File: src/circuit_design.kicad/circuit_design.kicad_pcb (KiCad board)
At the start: 2 copper layers, 205.7 x 170.8 mm, 183 parts, among them J1 CONN_BAT, Q1 BT134-600E, Q2 BT134-600E, Q3 BT134-600E, Q4 BT134-600E, U1 К176ИЕ12, U10 К155ЛА4, U11 К155ЛИ1, U12 К155ЛА1, U13 К155ИЕ5, U14 К155ЛЛ1, U15 К155ЛН1, U16 К155ЛИ1, U17 К155ТВ15, U18 К155ИЕ5, U19 К155ЛП5, U2 К155ЛП10, U20 К155ИВ1, U21 К155ИД7, U22 К155ИД4, U23 К155ЛН1, U24 К155ЛП10, U25 MOC3062M, U26 MOC3062M, U27 MOC3062M, U28 MOC3062M, U29 LM7806_TO220, U3 К155ЛЕ3, U30 SC6038, U31 К155ЛЕ1, U32 К155ЛН1, U33 К155ЛИ1, U34 К155ЛА4, U35 К155ТВ15, U36 К155ТЛ2, U37 4020, U38 LM7806_TO220, U39 К155ЛН1, U4 К155ЛН1, U5 К155ЛИ1, U6 К155ЛЛ1, U7 4020, U8 ICL7660, U9 К155ИЕ5, Y1 32768

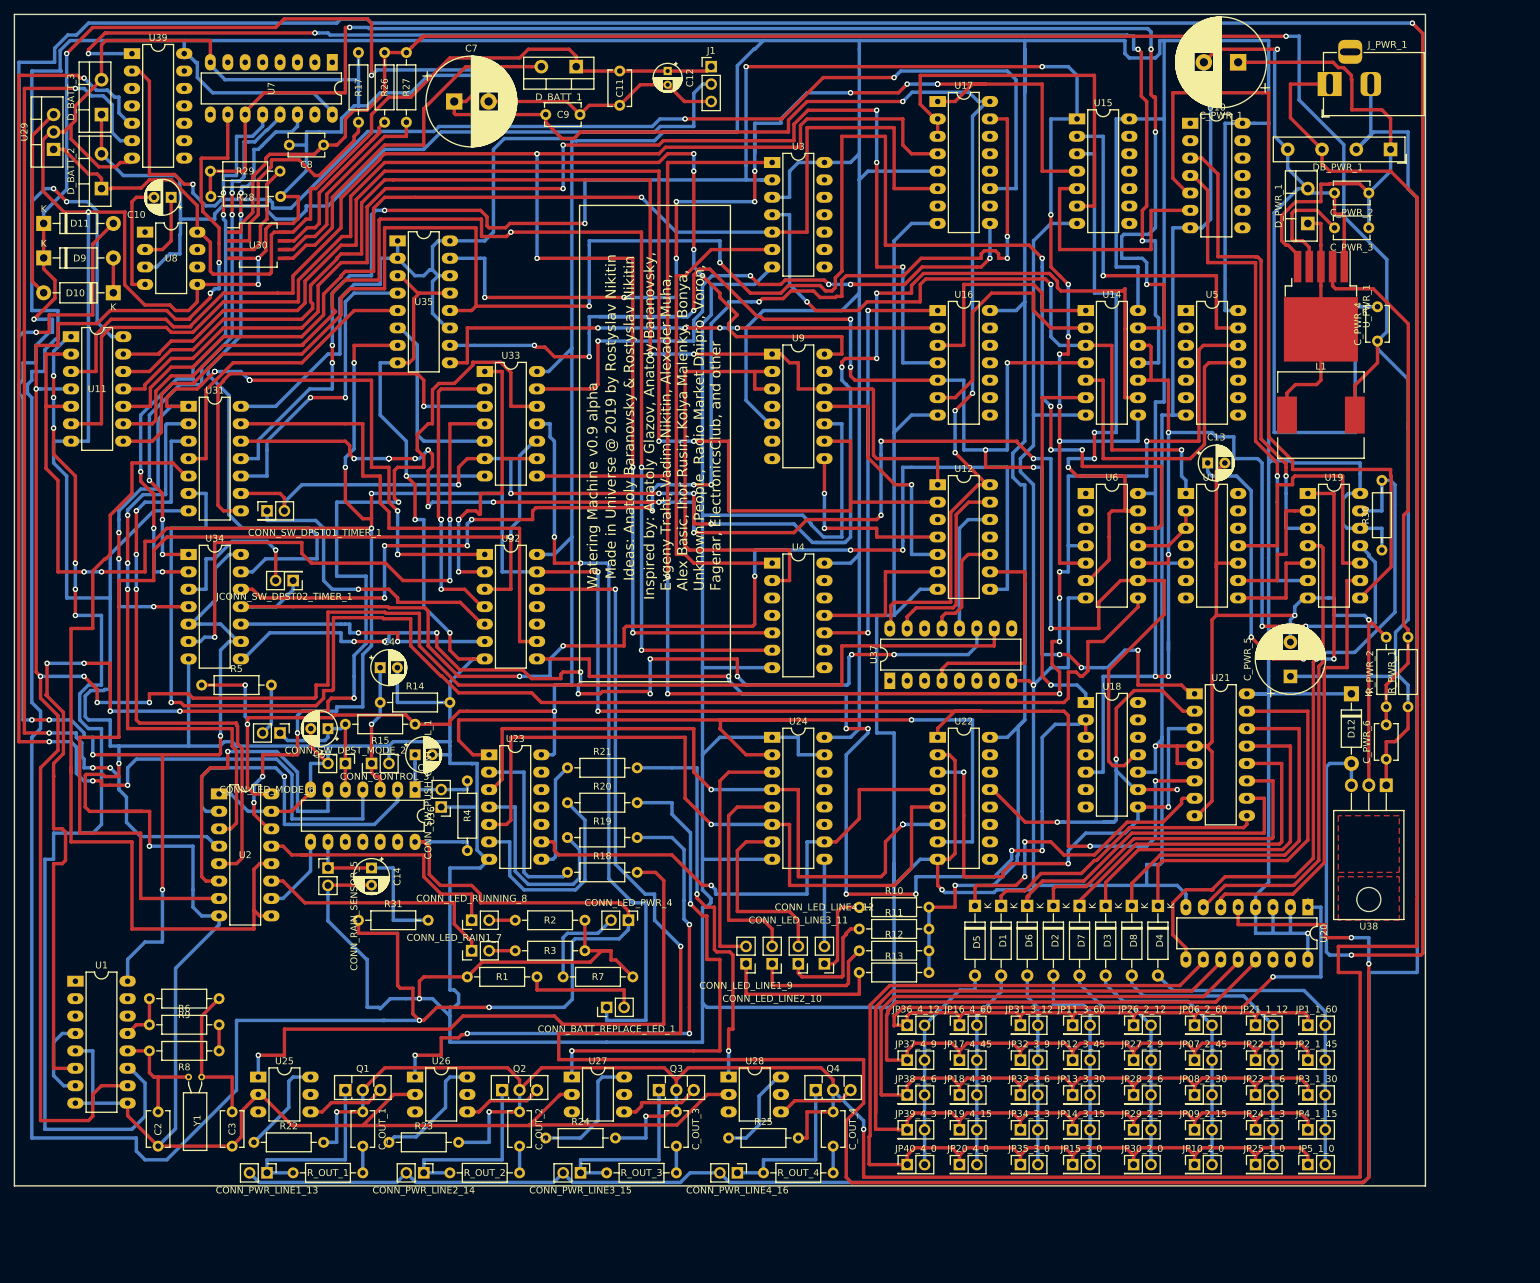
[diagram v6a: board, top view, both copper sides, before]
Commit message: The labels was updated:   - Was placed outside of the parts   - Was situated to be more readable
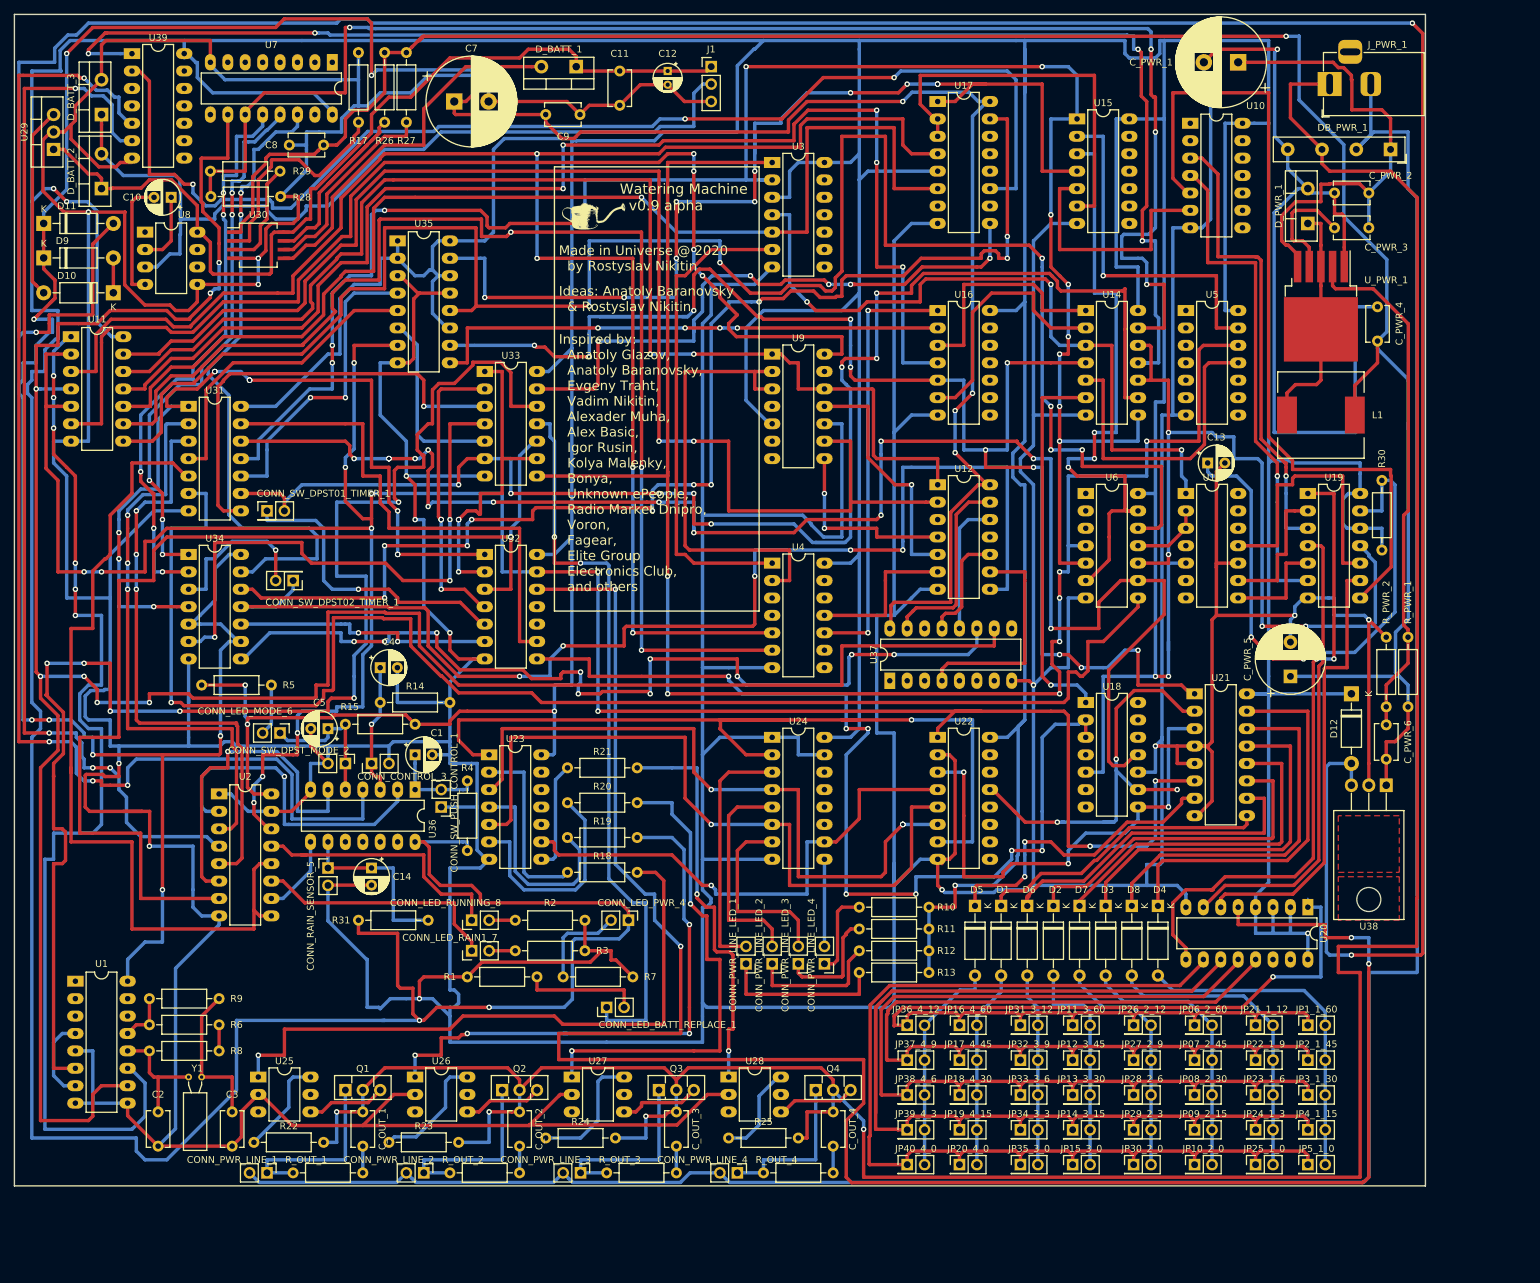
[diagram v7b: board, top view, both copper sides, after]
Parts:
- added G***: LOGO, circuit_design:logo, F.Cu at (127.6, 38.1)
- renumbered CONN_BATT_REPLACE_LED_1 to CONN_LED_BATT_REPLACE_1, CONN_PWR_LINE1_13 to CONN_PWR_LINE_1, CONN_PWR_LINE2_14 to CONN_PWR_LINE_2, CONN_PWR_LINE3_15 to CONN_PWR_LINE_3, CONN_PWR_LINE4_16 to CONN_PWR_LINE_4, CONN_LED_LINE1_9 to CONN_PWR_LINE_LED_1, CONN_LED_LINE2_10 to CONN_PWR_LINE_LED_2, CONN_LED_LINE3_11 to CONN_PWR_LINE_LED_3, CONN_LED_LINE4_12 to CONN_PWR_LINE_LED_4, JCONN_SW_DPST02_TIMER_1 to CONN_SW_DPST02_TIMER_1
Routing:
- net /D2: track 147.2 -> 144.4 mm
- net /D0: track 156.1 -> 153.3 mm
- net /D1: track 168.5 -> 165.7 mm
- net /D3: track 142.8 -> 140.1 mm
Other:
- board text added: "Inspired by: Anatoly Glazov, Anatoly Baranovsky, Evgeny Traht, Vadim Nikitin, Alexader Muha, Alex Basic, Igor Rusin, Kolya Malenky, Bonya, Unknown ePeople, Radio Market Dnipro, Voron, Fagear, Elite Group Electronics Club, and others"
- board text added: "Made in Universe @ 2020 by Rostyslav Nikitin"
- board text removed: "Inspired by: Anatoly Glazov, Anatoly Baranovsky, Evgeny Traht, Vadim Nikitin, Alexader Muha, Alex Basic, Ihor Rusin, Kolya Malenky, Bonya, Unknown People, Radio Market Dnipro, Voron, Fagerar, ElectronicsClub, and other"
- board text removed: "Made in Universe @ 2019 by Rostyslav Nikitin"

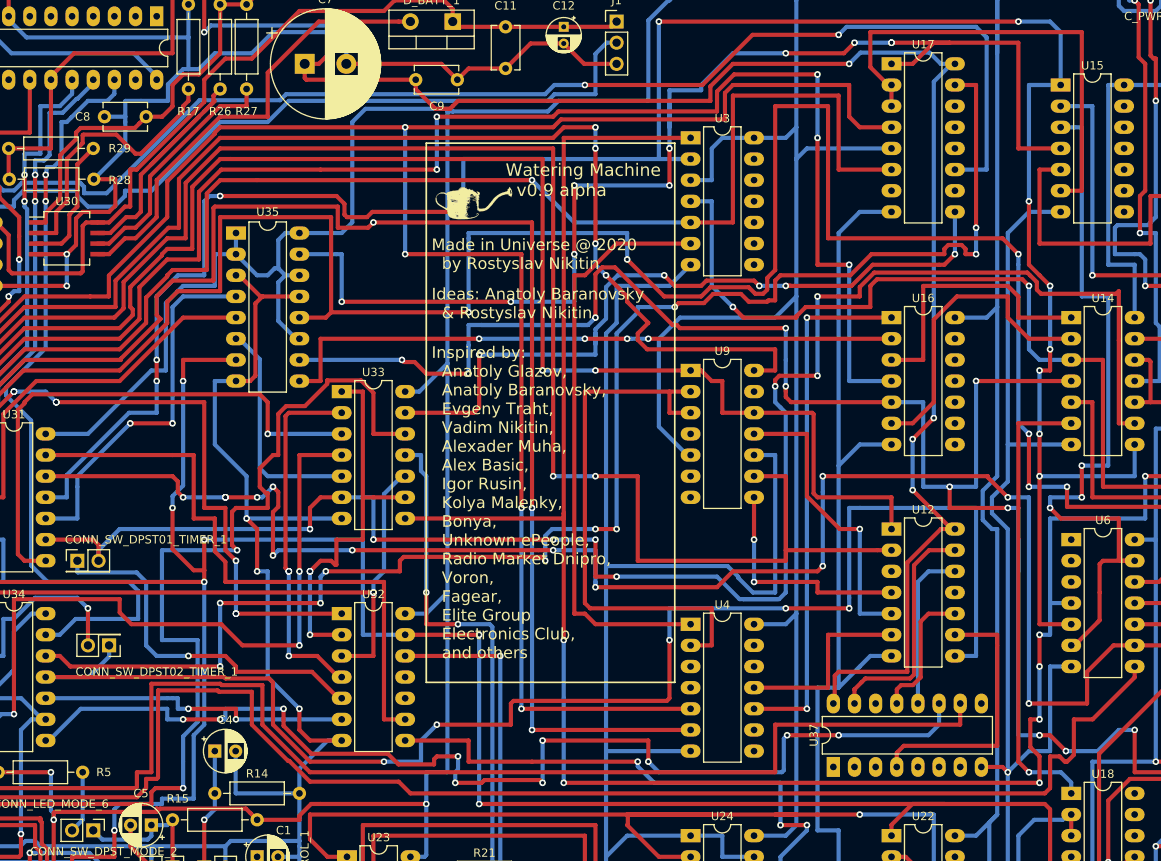
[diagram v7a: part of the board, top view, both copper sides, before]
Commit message: The git repository URI and the corresponding QR code was added to the silkography layer.
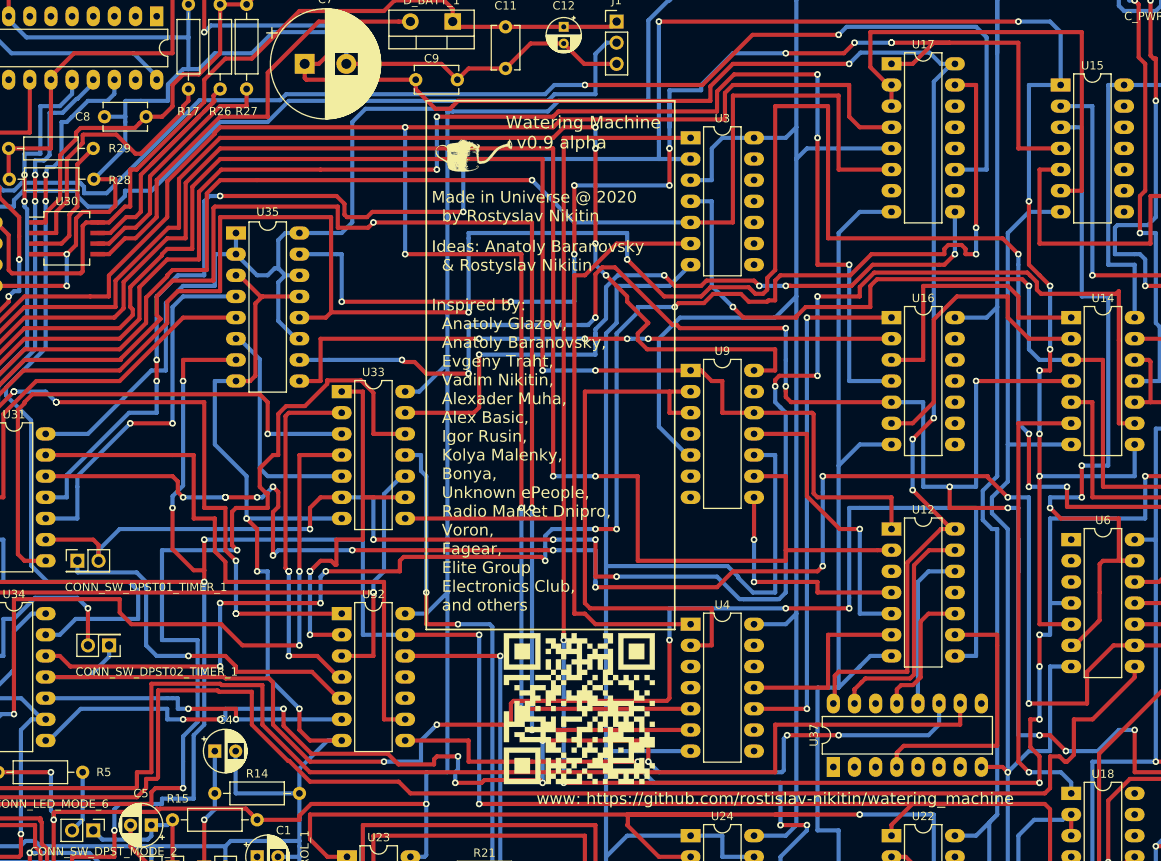
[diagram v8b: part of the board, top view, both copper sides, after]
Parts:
- added G***: LOGO, circuit_design:qrcode, F.Cu at (140.3, 99.1)
- moved G*** 5.72 mm to (127.6, 32.4)
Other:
- board text added: "www: https://github.com/rostislav-nikitin/watering_machine"
